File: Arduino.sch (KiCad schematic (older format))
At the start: 0 parts

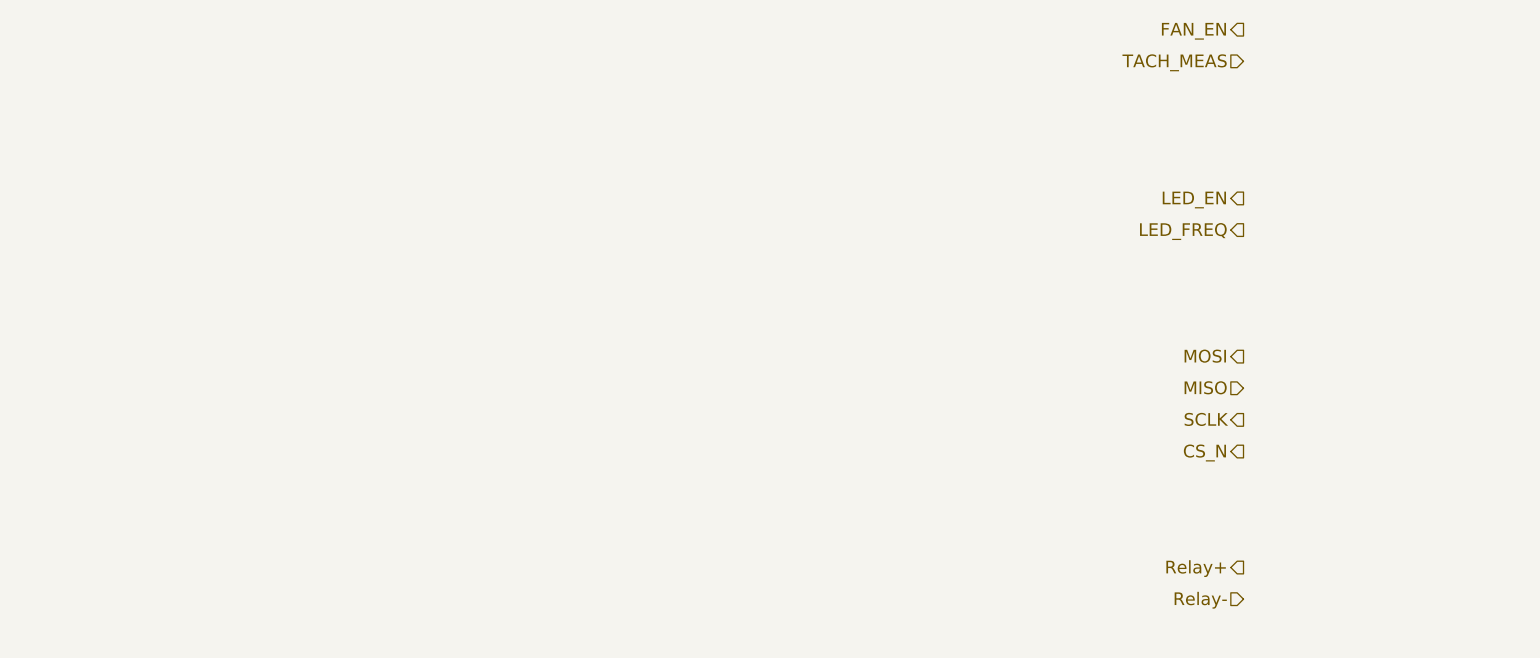
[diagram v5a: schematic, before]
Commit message: Added Arduino Block
Added Arduino Block and connected the top level of the schematic.
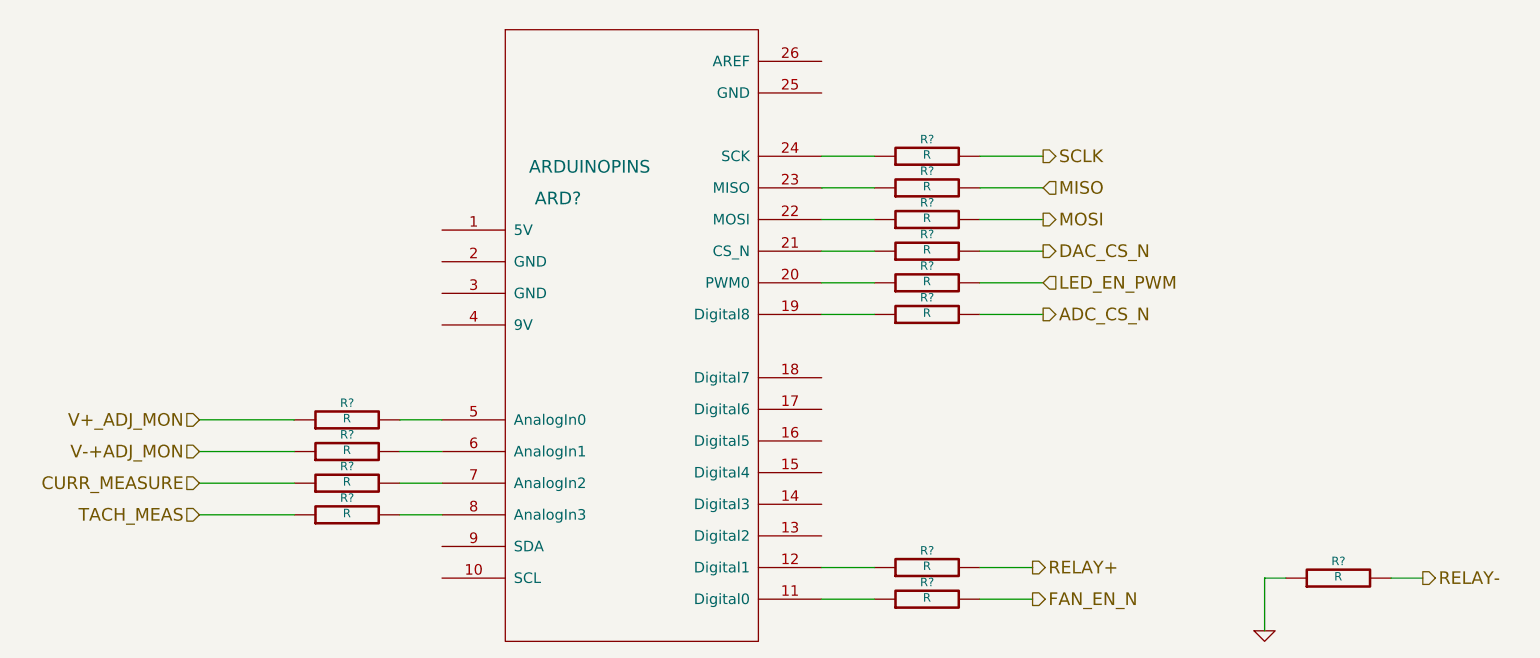
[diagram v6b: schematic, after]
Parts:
- added ARD?: ARDUINOPINS, symbol ARDUINOPINS
- added R? (x13): R, ~, symbol R
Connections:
- net MISO: now also R?.2
- net MOSI: now also R?.2
- net SCLK: now also R?.2
- net TACH_MEAS: now also R?.1
- new net: ARD?.11 (Digital0), R?.1
- new net: ARD?.12 (Digital1), R?.1
- new net: ARD?.19 (Digital8), R?.1
- new net: ARD?.20 (PWM0), R?.1
- new net: ARD?.21 (CS_N), R?.1
- new net: ARD?.22 (MOSI), R?.1
- new net: ARD?.23 (MISO), R?.1
- new net: ARD?.24 (SCK), R?.1
- new net: ARD?.5 (AnalogIn0), R?.2
- new net: ARD?.6 (AnalogIn1), R?.2
- new net: ARD?.7 (AnalogIn2), R?.2
- new net: ARD?.8 (AnalogIn3), R?.2
- new net ADC_CS_N: R?.2
- new net CURR_MEASURE: R?.1
- new net DAC_CS_N: R?.2
- new net FAN_EN_N: R?.2
- new net GND: R?.1
- new net LED_EN_PWM: R?.2
- new net RELAY+: R?.2
- new net RELAY-: R?.2
- new net V+_ADJ_MON: R?.1
- new net V-+ADJ_MON: R?.1

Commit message: Fan/Current Module Rework
Rework of the Fan/Current module
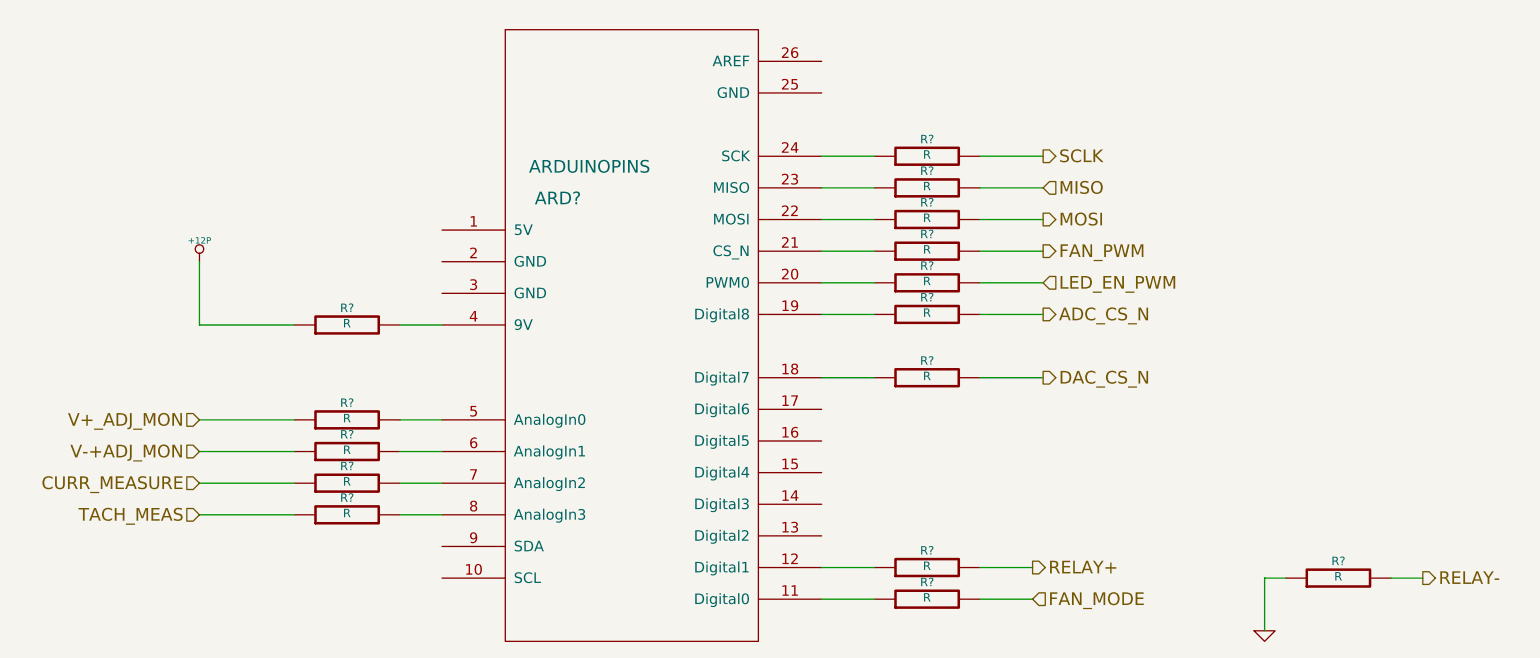
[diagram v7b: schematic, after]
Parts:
- added R? (x2): R, ~, symbol R
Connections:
- net at ARD?.11 (Digital0): now also R?.1; no longer R?.1
- net at ARD?.18 (Digital7): now also R?.1
- net at ARD?.21 (CS_N): now also R?.1; no longer R?.1
- net at ARD?.4 (9V): now also R?.2
- net FAN_EN_N renamed FAN_PWM
- new net +12P: R?.1
- new net FAN_MODE: R?.2
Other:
- moved on the sheet: R?
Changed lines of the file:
@@
 Text HLabel 6550 2200 2    60   Output ~ 0
 SCLK
+Text HLabel 6550 3250 2    60   Output ~ 0
+DAC_CS_N
 Text HLabel 6550 2650 2    60   Output ~ 0
-DAC_CS_N
-Text HLabel 6500 4300 2    60   Output ~ 0
-FAN_EN_N
+FAN_PWM
 Text HLabel 2550 3900 0    60   Input ~ 0
 TACH_MEAS
@@
 L R R?
 U 1 1 52472534
-P 6000 4300
-F 0 "R?" V 6080 4300 40  0000 C CNN
-F 1 "R" V 6007 4301 40  0000 C CNN
-F 2 "~" V 5930 4300 30  0000 C CNN
-F 3 "~" H 6000 4300 30  0000 C CNN
-	1    6000 4300
-	0    -1   -1   0
-$EndComp
-Wire Wire Line
-	6250 4300 6500 4300
+P 6000 2650
+F 0 "R?" V 6080 2650 40  0000 C CNN
+F 1 "R" V 6007 2651 40  0000 C CNN
+F 2 "~" V 5930 2650 30  0000 C CNN
+F 3 "~" H 6000 2650 30  0000 C CNN
+	1    6000 2650
+	0    -1   -1   0
+$EndComp
+Wire Wire Line
+	6250 2650 6550 2650
 $Comp
 L R R?
@@
 	7600 4200 7600 4450
 Wire Wire Line
-	5750 4300 5500 4300
+	5750 2650 5500 2650
 Wire Wire Line
 	5750 4150 5500 4150
@@
 L R R?
 U 1 1 52474586
-P 6000 2650
-F 0 "R?" V 6080 2650 40  0000 C CNN
-F 1 "R" V 6007 2651 40  0000 C CNN
-F 2 "~" V 5930 2650 30  0000 C CNN
-F 3 "~" H 6000 2650 30  0000 C CNN
-	1    6000 2650
+P 6000 3250
+F 0 "R?" V 6080 3250 40  0000 C CNN
+F 1 "R" V 6007 3251 40  0000 C CNN
+F 2 "~" V 5930 3250 30  0000 C CNN
+F 3 "~" H 6000 3250 30  0000 C CNN
+	1    6000 3250
 	0    -1   -1   0
 $EndComp
@@
 	5500 2500 5750 2500
 Wire Wire Line
-	5500 2650 5750 2650
-Wire Wire Line
-	6250 2650 6550 2650
+	5500 3250 5750 3250
+Wire Wire Line
+	6250 3250 6550 3250
 Wire Wire Line
 	6250 2500 6550 2500
@@
 Wire Wire Line
 	6250 2950 6550 2950
+Text HLabel 6500 4300 2    60   Input ~ 0
+FAN_MODE
+$Comp
+L R R?
+U 1 1 5246A39D
+P 6000 4300
+F 0 "R?" V 6080 4300 40  0000 C CNN
+F 1 "R" V 6007 4301 40  0000 C CNN
+F 2 "~" V 5930 4300 30  0000 C CNN
+F 3 "~" H 6000 4300 30  0000 C CNN
+	1    6000 4300
+	0    -1   -1   0
+$EndComp
+Wire Wire Line
+	5500 4300 5750 4300
+Wire Wire Line
+	6250 4300 6500 4300
+$Comp
+L R R?
+U 1 1 5246AAF7
+P 3250 3000
+F 0 "R?" V 3330 3000 40  0000 C CNN
+F 1 "R" V 3257 3001 40  0000 C CNN
+F 2 "~" V 3180 3000 30  0000 C CNN
+F 3 "~" H 3250 3000 30  0000 C CNN
+	1    3250 3000
+	0    -1   -1   0
+$EndComp
+Wire Wire Line
+	3500 3000 3700 3000
+$Comp
+L +12P #PWR?
+U 1 1 5246AB1D
+P 2550 2700
+F 0 "#PWR?" H 2550 2670 30  0001 C CNN
+F 1 "+12P" H 2550 2800 30  0000 C CNN
+F 2 "" H 2550 2700 60  0000 C CNN
+F 3 "" H 2550 2700 60  0000 C CNN
+	1    2550 2700
+	1    0    0    -1
+$EndComp
+Wire Wire Line
+	2550 2700 2550 3000
+Wire Wire Line
+	2550 3000 3000 3000
 $EndSCHEMATC

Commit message: Modified the Power Control module
Modified the Power Control module
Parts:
- added R? (x3): R, ~, symbol R
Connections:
- net GND: now also R?.1, R?.1
- net at ARD?.1 (5V): now also R?.2
- net at ARD?.2 (GND): now also R?.2
- net at ARD?.3 (GND): now also R?.2
- new net +5V: R?.1
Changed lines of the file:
@@
 $Descr A4 11693 8268
 encoding utf-8
-Sheet 9 9
+Sheet 8 9
 Title ""
-Date "28 sep 2013"
+Date "27 nov 2013"
 Rev ""
 Comp ""
@@
 L +12P #PWR?
 U 1 1 5246AB1D
-P 2550 2700
-F 0 "#PWR?" H 2550 2670 30  0001 C CNN
-F 1 "+12P" H 2550 2800 30  0000 C CNN
-F 2 "" H 2550 2700 60  0000 C CNN
-F 3 "" H 2550 2700 60  0000 C CNN
-	1    2550 2700
-	1    0    0    -1
-$EndComp
-Wire Wire Line
-	2550 2700 2550 3000
+P 2550 2800
+F 0 "#PWR?" H 2550 2770 30  0001 C CNN
+F 1 "+12P" H 2550 2900 30  0000 C CNN
+F 2 "" H 2550 2800 60  0000 C CNN
+F 3 "" H 2550 2800 60  0000 C CNN
+	1    2550 2800
+	1    0    0    -1
+$EndComp
+Wire Wire Line
+	2550 2800 2550 3000
 Wire Wire Line
 	2550 3000 3000 3000
+$Comp
+L R R?
+U 1 1 52958A33
+P 3250 2550
+F 0 "R?" V 3330 2550 40  0000 C CNN
+F 1 "R" V 3257 2551 40  0000 C CNN
+F 2 "~" V 3180 2550 30  0000 C CNN
+F 3 "~" H 3250 2550 30  0000 C CNN
+	1    3250 2550
+	0    -1   -1   0
+$EndComp
+Wire Wire Line
+	3500 2550 3700 2550
+$Comp
+L +5V #PWR?
+U 1 1 52958A5C
+P 2550 2350
+F 0 "#PWR?" H 2550 2440 20  0001 C CNN
+F 1 "+5V" H 2550 2440 30  0000 C CNN
+F 2 "" H 2550 2350 60  0000 C CNN
+F 3 "" H 2550 2350 60  0000 C CNN
+	1    2550 2350
+	1    0    0    -1
+$EndComp
+Wire Wire Line
+	3000 2550 2550 2550
+Wire Wire Line
+	2550 2550 2550 2350
+$Comp
+L R R?
+U 1 1 52958A96
+P 3250 2850
+F 0 "R?" V 3330 2850 40  0000 C CNN
+F 1 "R" V 3257 2851 40  0000 C CNN
+F 2 "~" V 3180 2850 30  0000 C CNN
+F 3 "~" H 3250 2850 30  0000 C CNN
+	1    3250 2850
+	0    -1   -1   0
+$EndComp
+$Comp
+L R R?
+U 1 1 52958AA1
+P 3250 2700
+F 0 "R?" V 3330 2700 40  0000 C CNN
+F 1 "R" V 3257 2701 40  0000 C CNN
+F 2 "~" V 3180 2700 30  0000 C CNN
+F 3 "~" H 3250 2700 30  0000 C CNN
+	1    3250 2700
+	0    -1   -1   0
+$EndComp
+Wire Wire Line
+	3500 2700 3700 2700
+Wire Wire Line
+	3500 2850 3700 2850
+Wire Wire Line
+	3000 2700 2750 2700
+Wire Wire Line
+	2750 2700 2750 2800
+Wire Wire Line
+	3000 2850 2900 2850
+Wire Wire Line
+	2900 2850 2900 2700
+Connection ~ 2900 2700
+$Comp
+L GND #PWR?
+U 1 1 52958B42
+P 2750 2800
+F 0 "#PWR?" H 2750 2800 30  0001 C CNN
+F 1 "GND" H 2750 2730 30  0001 C CNN
+F 2 "" H 2750 2800 60  0000 C CNN
+F 3 "" H 2750 2800 60  0000 C CNN
+	1    2750 2800
+	1    0    0    -1
+$EndComp
 $EndSCHEMATC
